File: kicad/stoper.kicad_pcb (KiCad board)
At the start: 2 copper layers, 29 parts

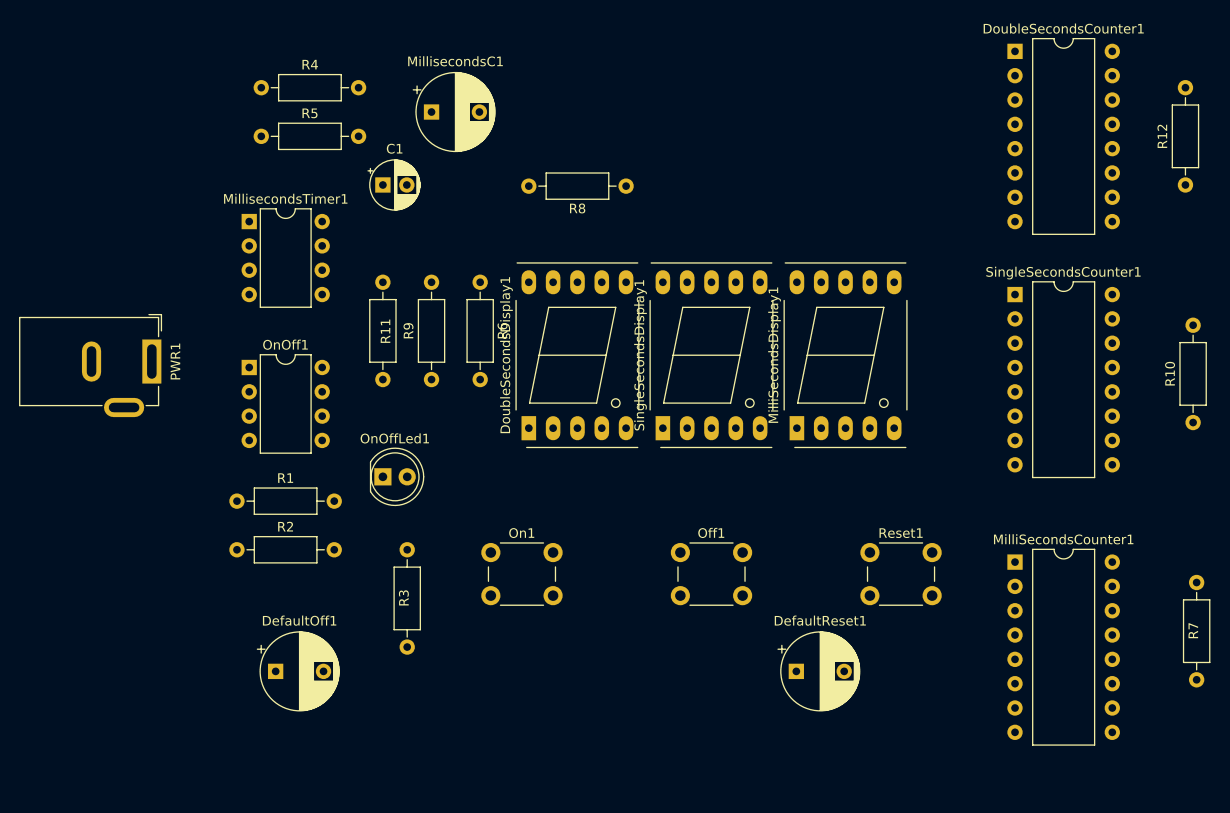
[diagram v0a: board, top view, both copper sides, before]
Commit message: save pcb layout draft v3, wiring finished
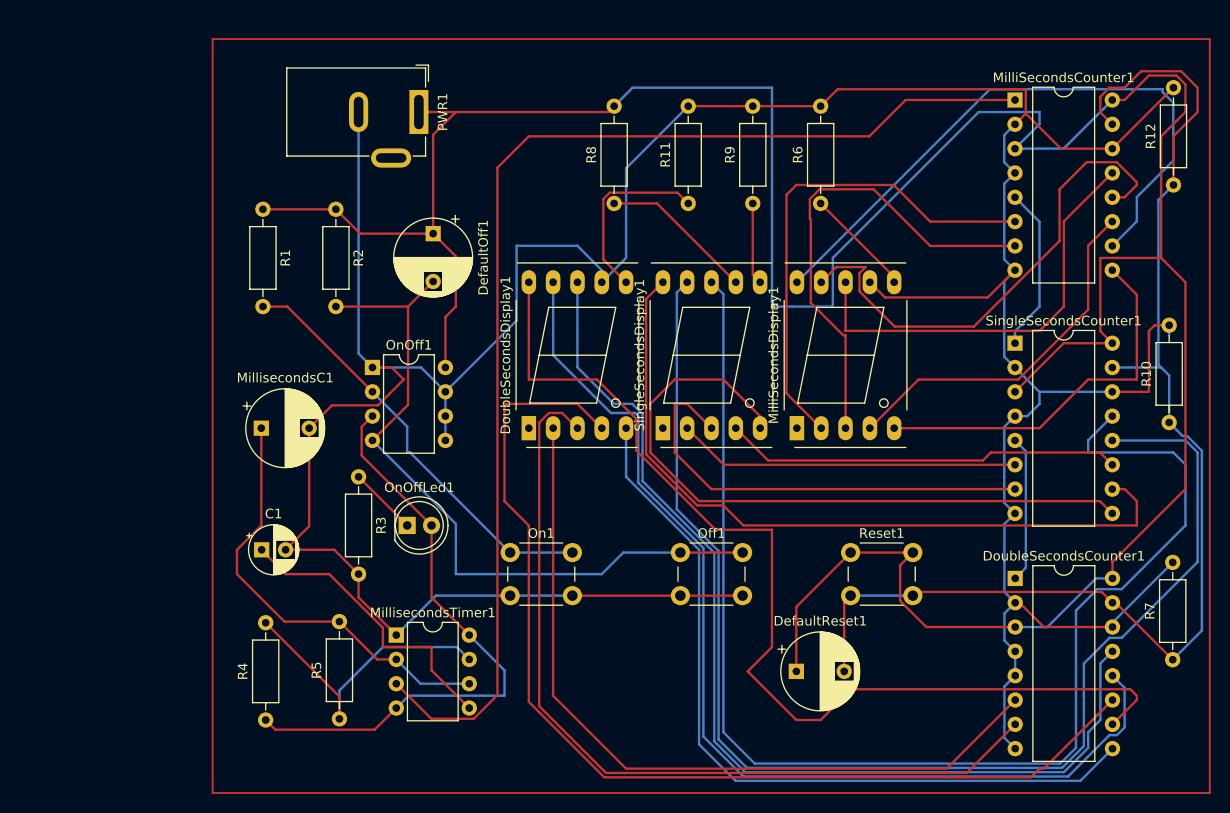
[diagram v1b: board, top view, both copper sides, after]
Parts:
- moved R4 66.0 mm to (74.1, 121.9), turned to 90 degrees
- moved R5 61.4 mm to (81.8, 121.8), turned to 90 degrees
- moved DoubleSecondsCounter1 55.0 mm to (152.4, 107.1)
- moved DefaultOff1 48.6 mm to (91.6, 71.1), turned to -90 degrees
- moved MilliSecondsCounter1 48.3 mm to (152.4, 57.2)
- moved MillisecondsTimer1 45.8 mm to (87.8, 113.0)
- moved C1 40.1 mm to (73.7, 104.1)
- moved R9 38.3 mm to (125.0, 68.0)
- moved PWR1 38.2 mm to (90.1, 58.4)
- moved MillisecondsC1 37.5 mm to (73.7, 91.4)
- moved R2 37.0 mm to (81.5, 68.6), turned to -90 degrees
- moved R11 36.8 mm to (118.2, 68.0)
- moved R6 36.5 mm to (132.1, 68.0), turned to 90 degrees
- moved R1 30.6 mm to (73.8, 68.6), turned to -90 degrees
- moved OnOff1 12.9 mm to (85.3, 85.1)
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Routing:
- net GND: track 0.00 -> 371.7 mm
- net /+9V: track 0.00 -> 311.4 mm
- net Net-(SingleSecondsCounter1-Pad13): track 0.00 -> 137.7 mm
- net Net-(SingleSecondsCounter1-Pad12): track 0.00 -> 136.1 mm
- net /ResetButtonIn1: track 0.00 -> 130.3 mm
- net /MilliSecondsPulse1: track 0.00 -> 125.2 mm
- net Net-(DoubleSecondsCounter1-Pad11): track 0.00 -> 110.9 mm
- net Net-(DoubleSecondsCounter1-Pad12): track 0.00 -> 109.2 mm
- net Net-(DoubleSecondsCounter1-Pad10): track 0.00 -> 108.2 mm
- net Net-(DoubleSecondsCounter1-Pad13): track 0.00 -> 107.6 mm
- net Net-(DoubleSecondsCounter1-Pad7): track 0.00 -> 89.4 mm
- net Net-(DoubleSecondsCounter1-Pad9): track 0.00 -> 82.3 mm
- net Net-(DoubleSecondsCounter1-Pad6): track 0.00 -> 82.3 mm
- net Net-(SingleSecondsCounter1-Pad10): track 0.00 -> 78.6 mm
- net Net-(DefaultOff1-Pad2): track 0.00 -> 75.2 mm
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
